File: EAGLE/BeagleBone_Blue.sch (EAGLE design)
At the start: 299 parts, among them J2 SERVO_HEADERS_8X, M1 JST_ZH_2, M2 JST_ZH_2, M3 JST_ZH_2, M4 JST_ZH_2, Q1 MOSFET-N, U1 TCAN1051HV, U10 TXS0108ERGYR, U13 EMMC, U2 SN74LV1T126DBVR, U3 TPD4S012DRY, U4 TPD4S012DRY, U5 24LC_32AT-I/OT, U6 SN74LVC1G07_DCK_5, U7 WL1835MODGBMOCT, U8 TPS2105_DBV_5, U9 TXS0108ERGYR, X2 SCHA5B0200, X3 USB1, X4 10118192-0001LF, Y1 24 MHz, Y2 32.768kHz

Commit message: Updates to silkscreen.
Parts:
- GND, WP: value TESTPAD/W_HOLE_1X1 -> GHI2_TESTPAD/W_HOLE_1X1; device GHI2:TESTPAD/W_HOLE_1X1 -> BeagleBone_Blue:GHI2_TESTPAD/W_HOLE_1X1
- J2: value SERVO_HEADERS_8X -> STRAWSON_EAGLE_LIB_SERVO_HEADERS_8X; device Strawson_Eagle_Lib:SERVO_HEADERS_8X -> BeagleBone_Blue:STRAWSON_EAGLE_LIB_SERVO_HEADERS_8X
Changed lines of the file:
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@@
 <setting verticaltext="up"/>
 </settings>
-<grid distance="0.05" unitdist="inch" unit="inch" style="lines" multiple="1" display="no" altdistance="0.01" altunitdist="inch" altunit="inch"/>
+<grid distance="0.1" unitdist="inch" unit="inch" style="lines" multiple="1" display="no" altdistance="0.01" altunitdist="inch" altunit="inch"/>
 <layers>
-<layer number="1" name="Top" color="4" fill="1" visible="no" active="no"/>
-<layer number="2" name="Route2" color="1" fill="3" visible="no" active="no"/>
-<layer number="3" name="Route3" color="4" fill="3" visible="no" active="no"/>
-<layer number="4" name="Route4" color="1" fill="4" visible="no" active="no"/>
-<layer number="5" name="Route5" color="4" fill="4" visible="no" active="no"/>
-<layer number="6" name="Route6" color="1" fill="8" visible="no" active="no"/>
-<layer number="7" name="Route7" color="4" fill="8" visible="no" active="no"/>
-<layer number="8" name="Route8" color="1" fill="2" visible="no" active="no"/>
-<layer number="9" name="Route9" color="4" fill="2" visible="no" active="no"/>
-<layer number="10" name="Route10" color="1" fill="7" visible="no" active="no"/>
-<layer number="11" name="Route11" color="4" fill="7" visible="no" active="no"/>
-<layer number="12" name="Route12" color="1" fill="5" visible="no" active="no"/>
-<layer number="13" name="Route13" color="4" fill="5" visible="no" active="no"/>
-<layer number="14" name="Route14" color="1" fill="6" visible="no" active="no"/>
-<layer number="15" name="Route15" color="4" fill="6" visible="no" active="no"/>
-<layer number="16" name="Bottom" color="1" fill="1" visible="no" active="no"/>
-<layer number="17" name="Pads" color="2" fill="1" visible="no" active="no"/>
-<layer number="18" name="Vias" color="2" fill="1" visible="no" active="no"/>
-<layer number="19" name="Unrouted" color="6" fill="1" visible="no" active="no"/>
-<layer number="20" name="Dimension" color="15" fill="1" visible="no" active="no"/>
-<layer number="21" name="tPlace" color="7" fill="1" visible="no" active="no"/>
-<layer number="22" name="bPlace" color="7" fill="1" visible="no" active="no"/>
-<layer number="23" name="tOrigins" color="15" fill="1" visible="no" active="no"/>
-<layer number="24" name="bOrigins" color="15" fill="1" visible="no" active="no"/>
-<layer number="25" name="tNames" color="7" fill="1" visible="no" active="no"/>
-<layer number="26" name="bNames" color="7" fill="1" visible="no" active="no"/>
-<layer number="27" name="tValues" color="7" fill="1" visible="no" active="no"/>
-<layer number="28" name="bValues" color="7" fill="1" visible="no" active="no"/>
+<layer number="1" name="Top" color="4" fill="1" visible="yes" active="no"/>
+<layer number="2" name="Route2" color="1" fill="3" visible="yes" active="no"/>
+<layer number="3" name="Route3" color="4" fill="3" visible="yes" active="no"/>
+<layer number="4" name="Route4" color="1" fill="4" visible="yes" active="no"/>
+<layer number="5" name="Route5" color="4" fill="4" visible="yes" active="no"/>
+<layer number="6" name="Route6" color="1" fill="8" visible="yes" active="no"/>
+<layer number="7" name="Route7" color="4" fill="8" visible="yes" active="no"/>
+<layer number="8" name="Route8" color="1" fill="2" visible="yes" active="no"/>
+<layer number="9" name="Route9" color="4" fill="2" visible="yes" active="no"/>
+<layer number="10" name="Route10" color="1" fill="7" visible="yes" active="no"/>
+<layer number="11" name="Route11" color="4" fill="7" visible="yes" active="no"/>
+<layer number="12" name="Route12" color="1" fill="5" visible="yes" active="no"/>
+<layer number="13" name="Route13" color="4" fill="5" visible="yes" active="no"/>
+<layer number="14" name="Route14" color="1" fill="6" visible="yes" active="no"/>
+<layer number="15" name="Route15" color="4" fill="6" visible="yes" active="no"/>
+<layer number="16" name="Bottom" color="1" fill="1" visible="yes" active="no"/>
+<layer number="17" name="Pads" color="2" fill="1" visible="yes" active="no"/>
+<layer number="18" name="Vias" color="2" fill="1" visible="yes" active="no"/>
+<layer number="19" name="Unrouted" color="6" fill="1" visible="yes" active="no"/>
+<layer number="20" name="Dimension" color="15" fill="1" visible="yes" active="no"/>
+<layer number="21" name="tPlace" color="7" fill="1" visible="yes" active="no"/>
+<layer number="22" name="bPlace" color="7" fill="1" visible="yes" active="no"/>
+<layer number="23" name="tOrigins" color="15" fill="1" visible="yes" active="no"/>
+<layer number="24" name="bOrigins" color="15" fill="1" visible="yes" active="no"/>
+<layer number="25" name="tNames" color="7" fill="1" visible="yes" active="no"/>
+<layer number="26" name="bNames" color="7" fill="1" visible="yes" active="no"/>
+<layer number="27" name="tValues" color="7" fill="1" visible="yes" active="no"/>
+<layer number="28" name="bValues" color="7" fill="1" visible="yes" active="no"/>
 <layer number="29" name="tStop" color="7" fill="3" visible="no" active="no"/>
 <layer number="30" name="bStop" color="7" fill="6" visible="no" active="no"/>
@@
 <layer number="35" name="tGlue" color="7" fill="4" visible="no" active="no"/>
 <layer number="36" name="bGlue" color="7" fill="5" visible="no" active="no"/>
-<layer number="37" name="tTest" color="7" fill="1" visible="no" active="no"/>
-<layer number="38" name="bTest" color="7" fill="1" visible="no" active="no"/>
+<layer number="37" name="tTest" color="7" fill="1" visible="yes" active="no"/>
+<layer number="38" name="bTest" color="7" fill="1" visible="yes" active="no"/>
 <layer number="39" name="tKeepout" color="4" fill="11" visible="no" active="no"/>
 <layer number="40" name="bKeepout" color="1" fill="11" visible="no" active="no"/>
@@
 <layer number="44" name="Drills" color="7" fill="1" visible="no" active="no"/>
 <layer number="45" name="Holes" color="7" fill="1" visible="no" active="no"/>
-<layer number="46" name="Milling" color="3" fill="1" visible="no" active="no"/>
-<layer number="47" name="Measures" color="7" fill="1" visible="no" active="no"/>
-<layer number="48" name="Document" color="7" fill="1" visible="no" active="no"/>
-<layer number="49" name="Reference" color="7" fill="1" visible="no" active="no"/>
-<layer number="50" name="dxf" color="7" fill="1" visible="no" active="no"/>
-<layer number="51" name="tDocu" color="7" fill="1" visible="no" active="no"/>
-<layer number="52" name="bDocu" color="7" fill="1" visible="no" active="no"/>
-<layer number="53" name="tGND_GNDA" color="7" fill="9" visible="no" active="no"/>
-<layer number="54" name="bGND_GNDA" color="1" fill="9" visible="no" active="no"/>
-<layer number="56" name="wert" color="7" fill="1" visible="no" active="no"/>
-<layer number="57" name="tCAD" color="7" fill="1" visible="no" active="no"/>
-<layer number="59" name="tCarbon" color="7" fill="1" visible="no" active="no"/>
-<layer number="60" name="bCarbon" color="7" fill="1" visible="no" active="no"/>
+<layer number="46" name="Milling" color="3" fill="1" visible="yes" active="no"/>
+<layer number="47" name="Measures" color="7" fill="1" visible="yes" active="no"/>
+<layer number="48" name="Document" color="7" fill="1" visible="yes" active="no"/>
+<layer number="49" name="Reference" color="7" fill="1" visible="yes" active="no"/>
+<layer number="50" name="dxf" color="7" fill="1" visible="yes" active="no"/>
+<layer number="51" name="tDocu" color="7" fill="1" visible="yes" active="no"/>
+<layer number="52" name="bDocu" color="7" fill="1" visible="yes" active="no"/>
+<layer number="53" name="tGND_GNDA" color="7" fill="9" visible="yes" active="no"/>
+<layer number="54" name="bGND_GNDA" color="1" fill="9" visible="yes" active="no"/>
+<layer number="56" name="wert" color="7" fill="1" visible="yes" active="no"/>
+<layer number="57" name="tCAD" color="7" fill="1" visible="yes" active="no"/>
+<layer number="59" name="tCarbon" color="7" fill="1" visible="yes" active="no"/>
+<layer number="60" name="bCarbon" color="7" fill="1" visible="yes" active="no"/>
 <layer number="90" name="Modules" color="5" fill="1" visible="yes" active="yes"/>
 <layer number="91" name="Nets" color="2" fill="1" visible="yes" active="yes"/>
@@
 <part name="M4" library="Strawson_Eagle_Lib" deviceset="JST_ZH_2" device="" value="JST_ZH_2"/>
 <part name="M3" library="Strawson_Eagle_Lib" deviceset="JST_ZH_2" device="" value="JST_ZH_2"/>
-<part name="J2" library="Strawson_Eagle_Lib" deviceset="SERVO_HEADERS_8X" device=""/>
+<part name="J2" library="BeagleBone_Blue" deviceset="STRAWSON_EAGLE_LIB_SERVO_HEADERS_8X" device=""/>
 <part name="GND19" library="SparkFun-Aesthetics" deviceset="GND" device=""/>
 <part name="GND27" library="SparkFun-Aesthetics" deviceset="GND" device=""/>
@@
 <part name="SUPPLY9" library="GHI-PowerGoundSupply" deviceset="CGND" device=""/>
 <part name="SUPPLY85" library="GHI-PowerGoundSupply" deviceset="CGND" device=""/>
-<part name="WP" library="GHI2" deviceset="TESTPAD/W_HOLE_1X1" device=""/>
+<part name="WP" library="BeagleBone_Blue" deviceset="GHI2_TESTPAD/W_HOLE_1X1" device=""/>
 <part name="MGT1" library="BeagleBoneBlack" deviceset="MOUNTING_HOLE" device=""/>
 <part name="MGT2" library="BeagleBoneBlack" deviceset="MOUNTING_HOLE" device=""/>
@@
 <part name="I2C" library="Strawson_Eagle_Lib" deviceset="JST_SH_4" device=""/>
 <part name="UT5" library="Strawson_Eagle_Lib" deviceset="JST_SH_4" device=""/>
-<part name="GND" library="GHI2" deviceset="TESTPAD/W_HOLE_1X1" device=""/>
+<part name="GND" library="BeagleBone_Blue" deviceset="GHI2_TESTPAD/W_HOLE_1X1" device=""/>
 <part name="C59" library="SparkFun-Capacitors" deviceset="CAP" device="0805" value="10uF"/>
 <part name="C60" library="SparkFun-Capacitors" deviceset="CAP" device="0805" value="10uF"/>

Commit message: Updated layout.
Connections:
- net LED_GRN: now also GP1.6; no longer GP1.5
- net LED_RED: now also GP1.5; no longer GP1.6
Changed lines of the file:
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@@
 <setting verticaltext="up"/>
 </settings>
-<grid distance="0.1" unitdist="inch" unit="inch" style="lines" multiple="1" display="no" altdistance="0.01" altunitdist="inch" altunit="inch"/>
+<grid distance="0.05" unitdist="inch" unit="inch" style="lines" multiple="1" display="no" altdistance="0.01" altunitdist="inch" altunit="inch"/>
 <layers>
 <layer number="1" name="Top" color="4" fill="1" visible="yes" active="no"/>
@@
 </segment>
 <segment>
-<pinref part="GP1" gate="G$1" pin="5"/>
-<wire x1="146.05" y1="13.97" x2="132.08" y2="13.97" width="0.1524" layer="91"/>
-<label x="133.35" y="13.97" size="1.778" layer="95"/>
+<pinref part="GP1" gate="G$1" pin="6"/>
+<wire x1="146.05" y1="11.43" x2="132.08" y2="11.43" width="0.1524" layer="91"/>
+<label x="133.35" y="11.43" size="1.778" layer="95"/>
 </segment>
 </net>
@@
 </segment>
 <segment>
-<pinref part="GP1" gate="G$1" pin="6"/>
-<wire x1="146.05" y1="11.43" x2="132.08" y2="11.43" width="0.1524" layer="91"/>
-<label x="133.35" y="11.43" size="1.778" layer="95"/>
-</segment>
-</net>
+<pinref part="GP1" gate="G$1" pin="5"/>
+<wire x1="146.05" y1="13.97" x2="132.08" y2="13.97" width="0.1524" layer="91"/>
+<label x="133.35" y="13.97" size="1.778" layer="95"/>
+</segment>
+</net>

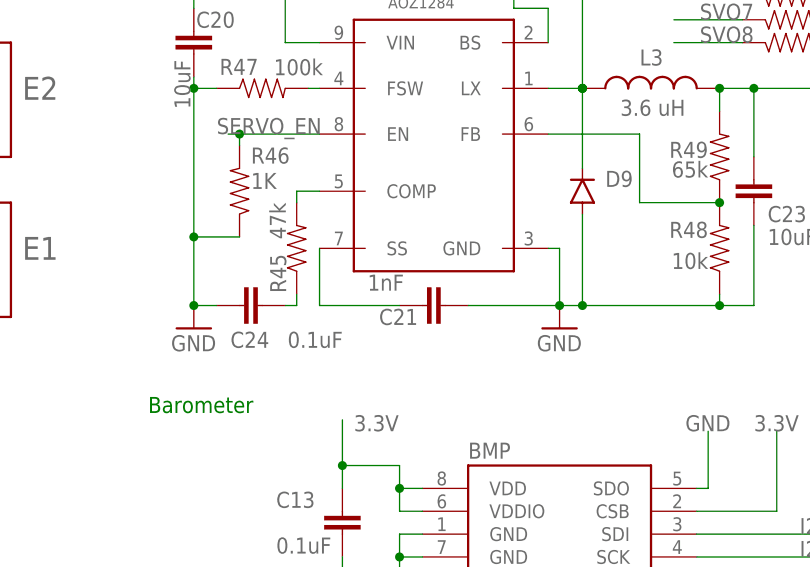
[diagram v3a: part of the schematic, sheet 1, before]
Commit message: Updated C21 value; Cleaned up silk screen.
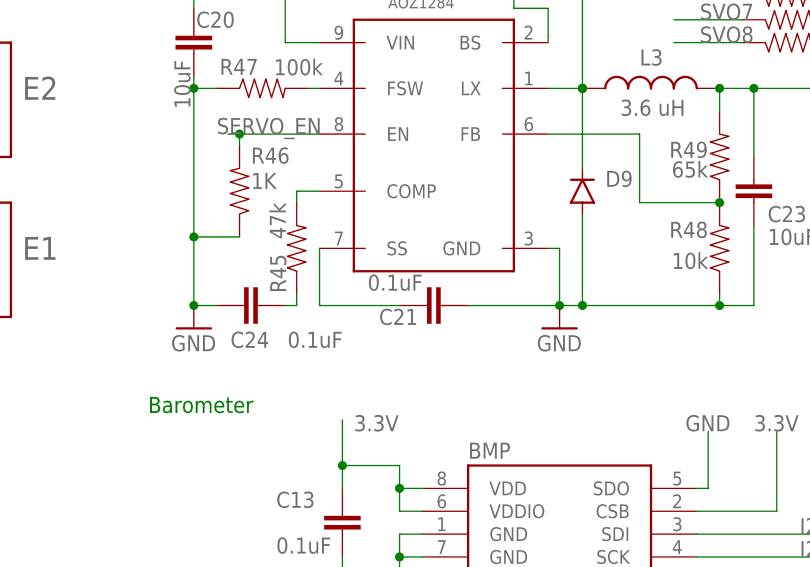
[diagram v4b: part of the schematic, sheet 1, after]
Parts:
- C21: value 1nF -> 0.1uF
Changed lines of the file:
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@@
 <part name="6VREG" library="Strawson_Eagle_Lib" deviceset="AOZ1284" device=""/>
 <part name="C20" library="SparkFun-Capacitors" deviceset="CAP" device="0805" value="10uF"/>
-<part name="C21" library="Strawson_Eagle_Lib" deviceset="CAP" device="0402-CAP" value="1nF"/>
+<part name="C21" library="Strawson_Eagle_Lib" deviceset="CAP" device="0402-CAP" value="0.1uF"/>
 <part name="C22" library="Strawson_Eagle_Lib" deviceset="CAP" device="0402-CAP" value="0.1uF"/>
 <part name="R47" library="Strawson_Eagle_Lib" deviceset="RESISTOR" device="0402-RES" value="100k"/>
